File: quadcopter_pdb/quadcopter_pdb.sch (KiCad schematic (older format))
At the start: 25 parts, among them P1 XT60_SMT, P10 CONN_01X03, P11 CONN_01X03, P12 CONN_01X03, P13 CONN_02X25, P14 CONN_02X25, P2 XT60_SMT, P3 XT60_SMT, P4 CONN_01X07, P5 CONN_01X02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

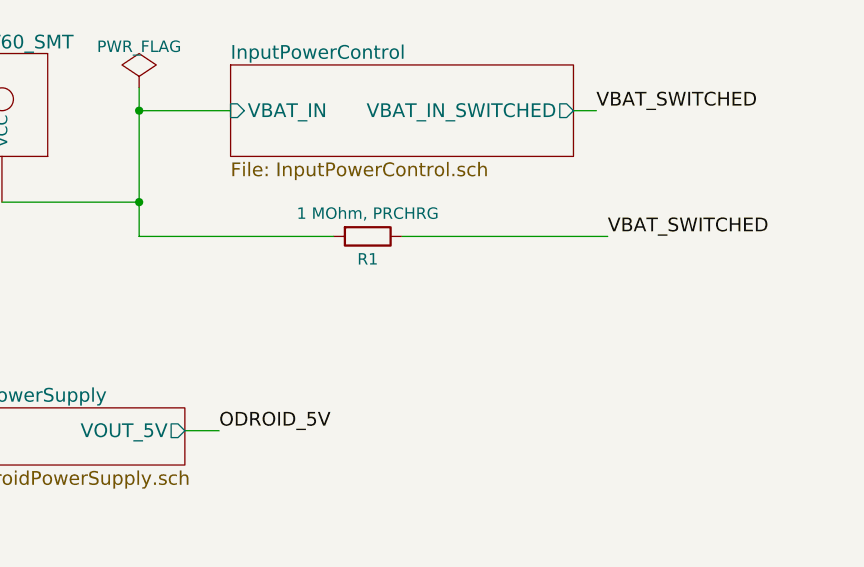
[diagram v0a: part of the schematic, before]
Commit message: Updating silkscreen on Quadcopter PDB.
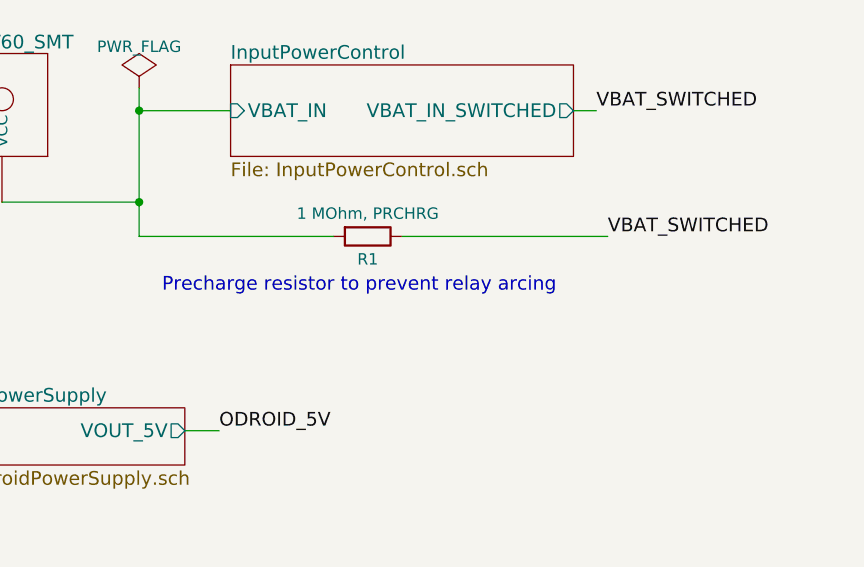
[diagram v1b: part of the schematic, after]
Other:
- note added: "Precharge resistor to prevent relay arcing"
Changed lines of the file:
@@
 Sheet 1 3
 Title ""
-Date ""
-Rev ""
+Date "2017-05-26"
+Rev "1.3"
 Comp ""
-Comment1 ""
-Comment2 ""
-Comment3 ""
-Comment4 ""
+Comment1 "QUAD001-001"
+Comment2 "QUAD001-101"
+Comment3 "Abhimanyu Ghosh"
+Comment4 "Abhimanyu Ghosh"
 $EndDescr
 $Comp
@@
 Text Label 8400 3900 0    60   ~ 0
 VBAT_SWITCHED
+Text Notes 2550 2100 0    60   ~ 0
+Precharge resistor to prevent relay arcing
 $EndSCHEMATC

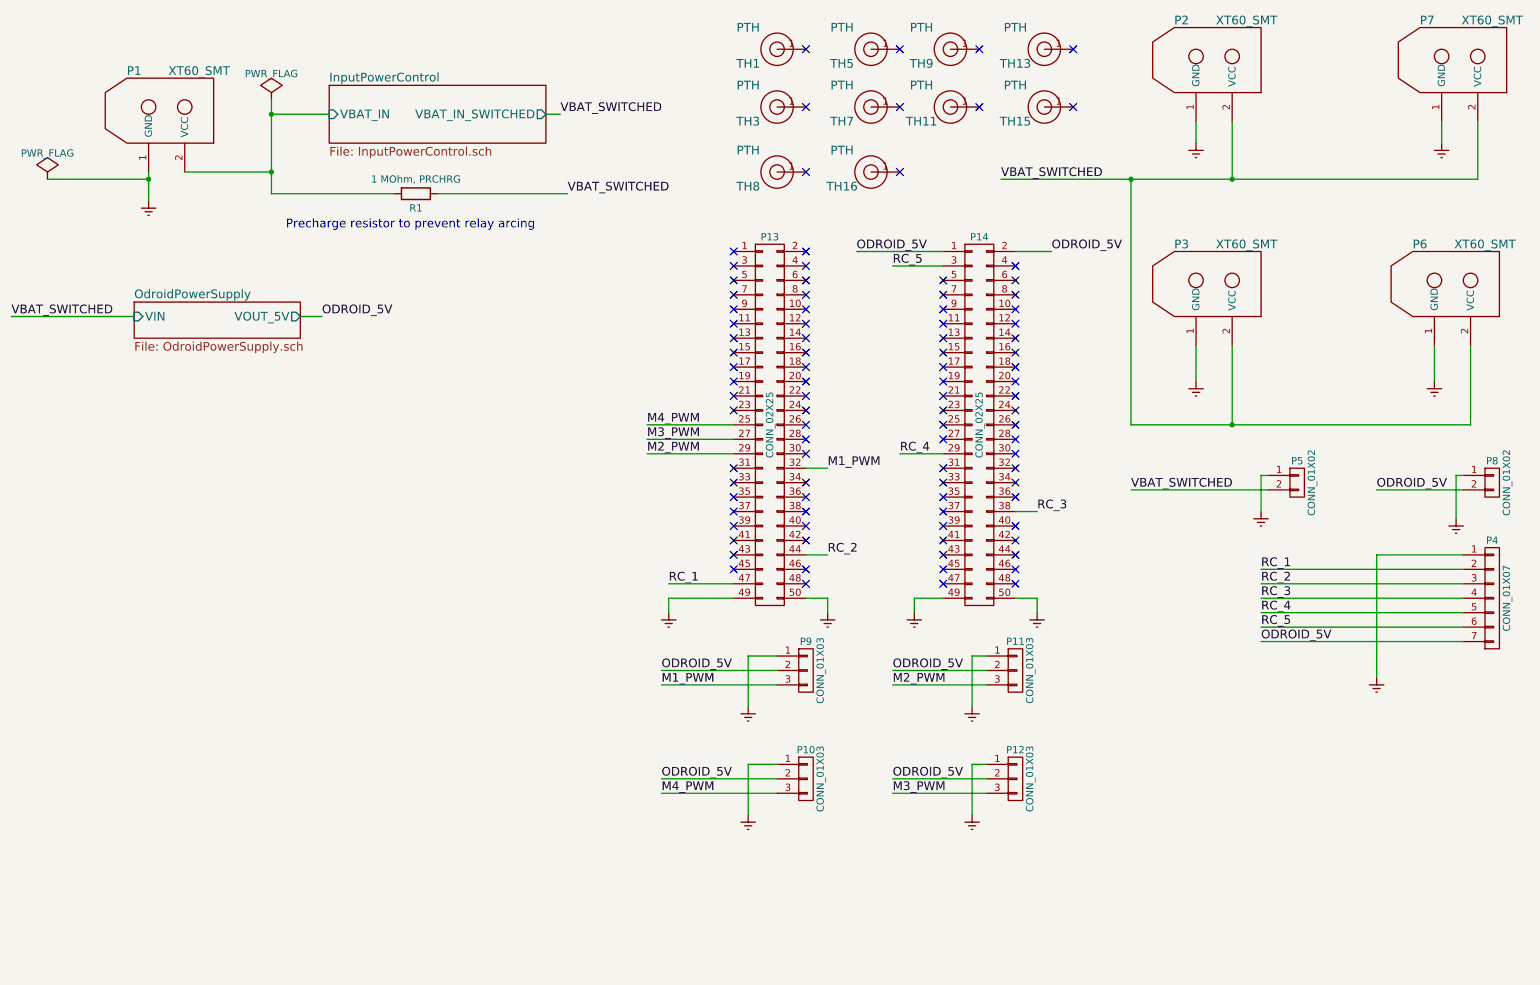
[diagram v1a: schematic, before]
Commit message: Updating Quadcopter PDB to latest combined design capable of accomodating AP or STM32 systems.
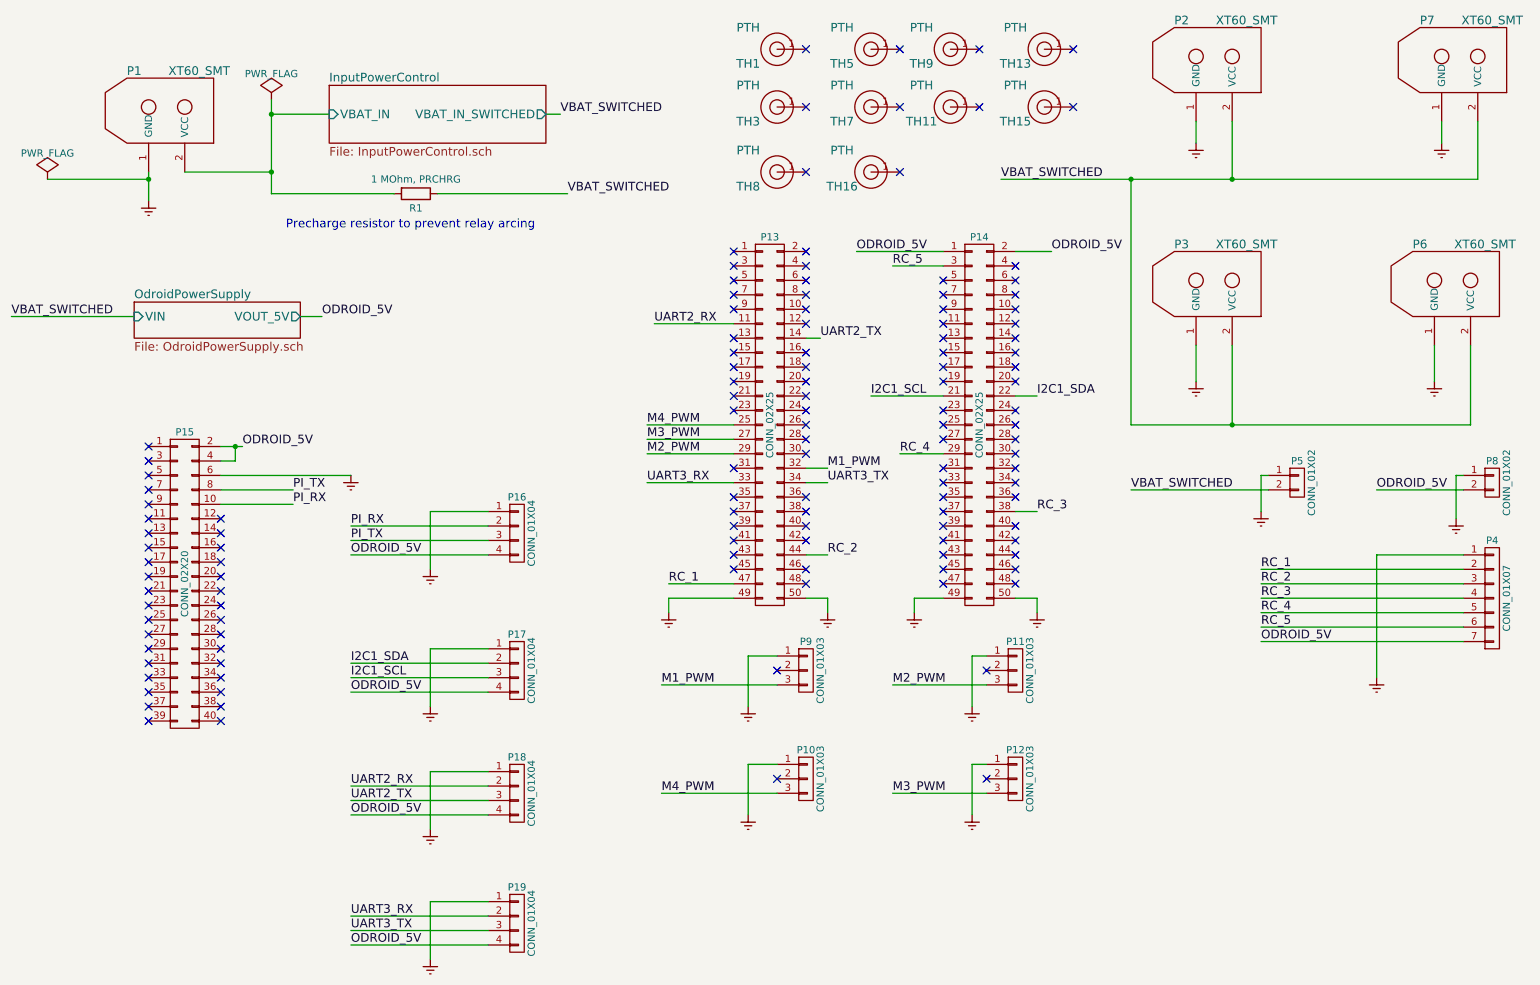
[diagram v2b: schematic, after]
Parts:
- added P15: CONN_02X20, Pin_Headers:Pin_Header_Straight_2x20, symbol CONN_02X20
- added P16, P17, P18, P19: CONN_01X04, Pin_Headers:Pin_Header_Straight_1x04, symbol CONN_01X04
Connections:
- net Earth: now also P15.6 (P6), P16.1 (P1), P17.1 (P1), P18.1 (P1), P19.1 (P1)
- net ODROID_5V: now also P15.2 (P2), P15.4 (P4), P16.4 (P4), P17.4 (P4), P18.4 (P4), P19.4 (P4); no longer P10.2 (P2), P11.2 (P2), P12.2 (P2), P9.2 (P2)
- net UART2_RX: now reaches P13.11 (P11)
- net UART2_RX: now also P18.2 (P2)
- net UART2_TX: now reaches P13.14 (P14)
- net UART2_TX: now also P18.3 (P3)
- net UART3_RX: now reaches P13.33 (P33)
- net UART3_RX: now also P19.2 (P2)
- net UART3_TX: now reaches P13.34 (P34)
- net UART3_TX: now also P19.3 (P3)
- net I2C1_SCL: now reaches P14.21 (P21)
- net I2C1_SCL: now also P17.3 (P3)
- net I2C1_SDA: now reaches P14.22 (P22)
- net I2C1_SDA: now also P17.2 (P2)
- new net PI_RX: P15.10 (P10), P16.2 (P2)
- new net PI_TX: P15.8 (P8), P16.3 (P3)
- no-connect marks 95 -> 128

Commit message: One last update.
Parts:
- added TH10, TH2, TH4, TH6: PTH, Mounting_Holes:MountingHole_3mm, symbol PTH
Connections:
- no-connect marks 128 -> 132
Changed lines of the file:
@@
 Wire Wire Line
 	6150 3850 6300 3850
+$Comp
+L PTH TH2
+U 1 1 592ED0E3
+P 1050 6050
+F 0 "TH2" H 850 5950 60  0000 C CNN
+F 1 "PTH" H 850 6200 60  0000 C CNN
+F 2 "Mounting_Holes:MountingHole_3mm" H 1050 6050 60  0001 C CNN
+F 3 "" H 1050 6050 60  0000 C CNN
+	1    1050 6050
+	1    0    0    -1
+$EndComp
+NoConn ~ 1250 6500
+NoConn ~ 1250 6050
+NoConn ~ 1900 6500
+NoConn ~ 1900 6050
+$Comp
+L PTH TH4
+U 1 1 592EEF36
+P 1050 6500
+F 0 "TH4" H 850 6400 60  0000 C CNN
+F 1 "PTH" H 850 6650 60  0000 C CNN
+F 2 "Mounting_Holes:MountingHole_3mm" H 1050 6500 60  0001 C CNN
+F 3 "" H 1050 6500 60  0000 C CNN
+	1    1050 6500
+	1    0    0    -1
+$EndComp
+$Comp
+L PTH TH10
+U 1 1 592EEFCE
+P 1700 6500
+F 0 "TH10" H 1500 6400 60  0000 C CNN
+F 1 "PTH" H 1500 6650 60  0000 C CNN
+F 2 "Mounting_Holes:MountingHole_3mm" H 1700 6500 60  0001 C CNN
+F 3 "" H 1700 6500 60  0000 C CNN
+	1    1700 6500
+	1    0    0    -1
+$EndComp
+$Comp
+L PTH TH6
+U 1 1 592EF075
+P 1700 6050
+F 0 "TH6" H 1500 5950 60  0000 C CNN
+F 1 "PTH" H 1500 6200 60  0000 C CNN
+F 2 "Mounting_Holes:MountingHole_3mm" H 1700 6050 60  0001 C CNN
+F 3 "" H 1700 6050 60  0000 C CNN
+	1    1700 6050
+	1    0    0    -1
+$EndComp
 $EndSCHEMATC
